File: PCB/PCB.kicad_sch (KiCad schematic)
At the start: 114 parts, among them J1 Termocouple_2, J10 2x5_2.54mm, J12 SSR2, J13 14x1-2.54mm, J14 USB_C_Receptacle_USB2.0, J2 PWR_IN, J3 Conn_01x02_Pin, J4 4x1-2.54mm, J5 Termocouple_1, J6 OUT2, J7 OUT1, J8 SSR1, Q1 BC817, Q2 BC817, Q3 BC817, Q4 BC817, Q5 AP30N03DF, SW1 SW_DPDT, SW2 SW_SPST, U1 MAX31855KASA, U2 MAX31855KASA, U4 MP2303ADN, U5 STM32F411CEUx, U6 CH340G, U7 W25Q16JVSNIQ, Y1 12MHz, Y3 12MHz

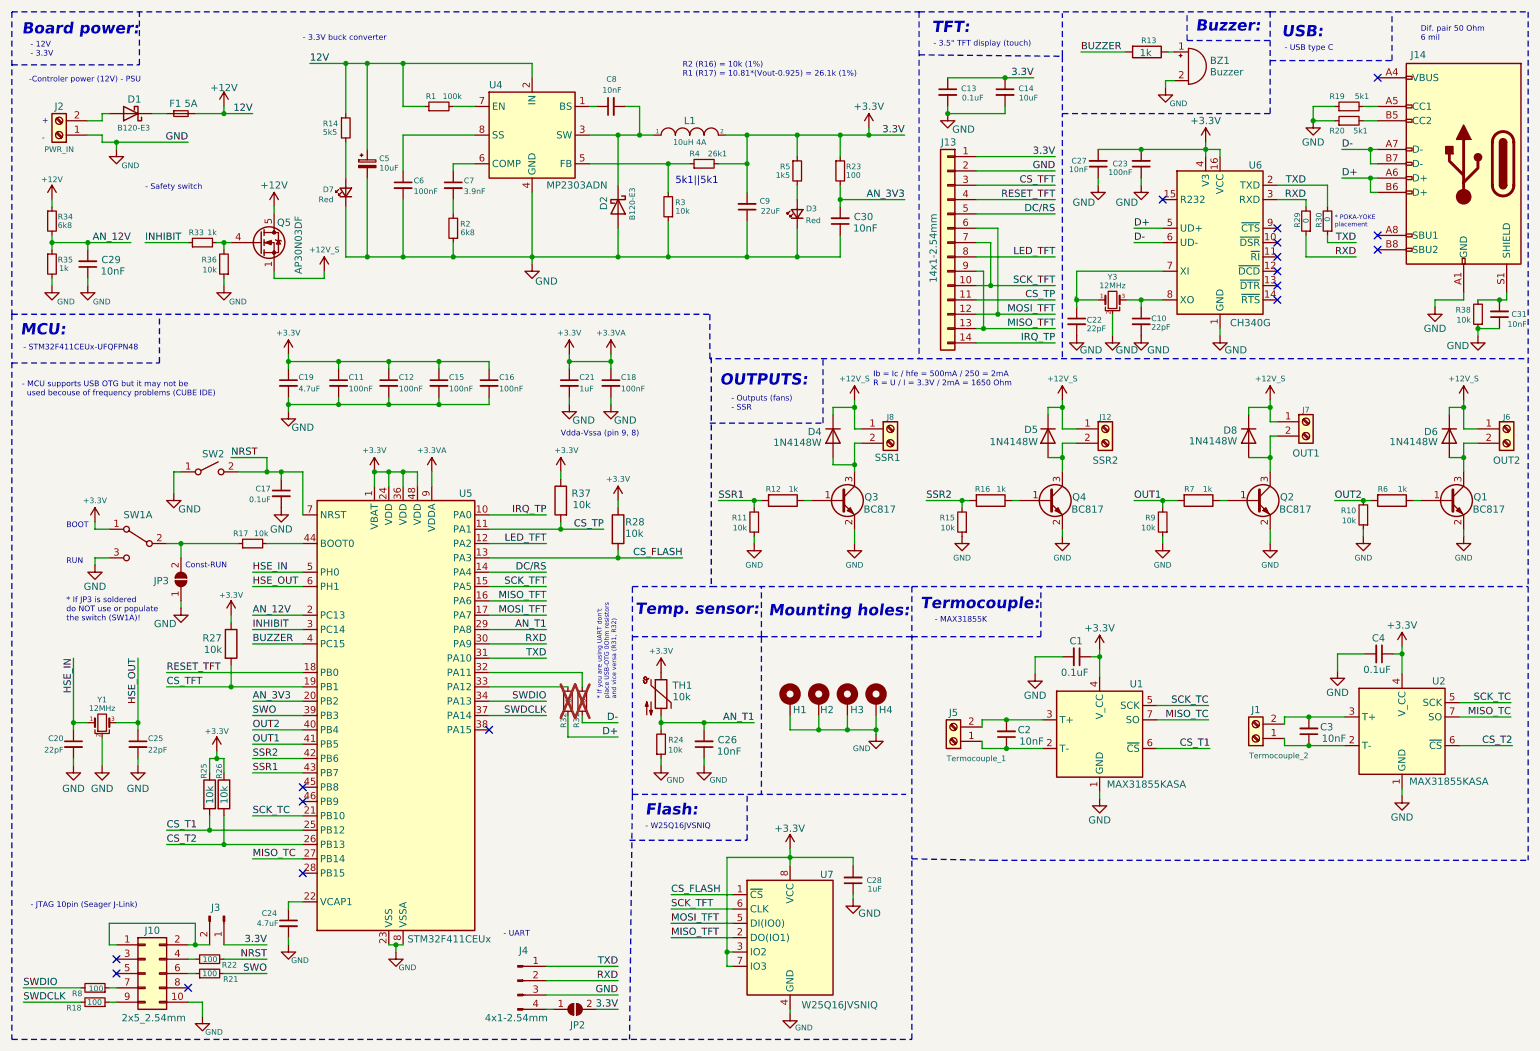
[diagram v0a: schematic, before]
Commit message: PCB done and ordered, touch screen and TFT works, flash works, EdternalLoader, GUI partialy done
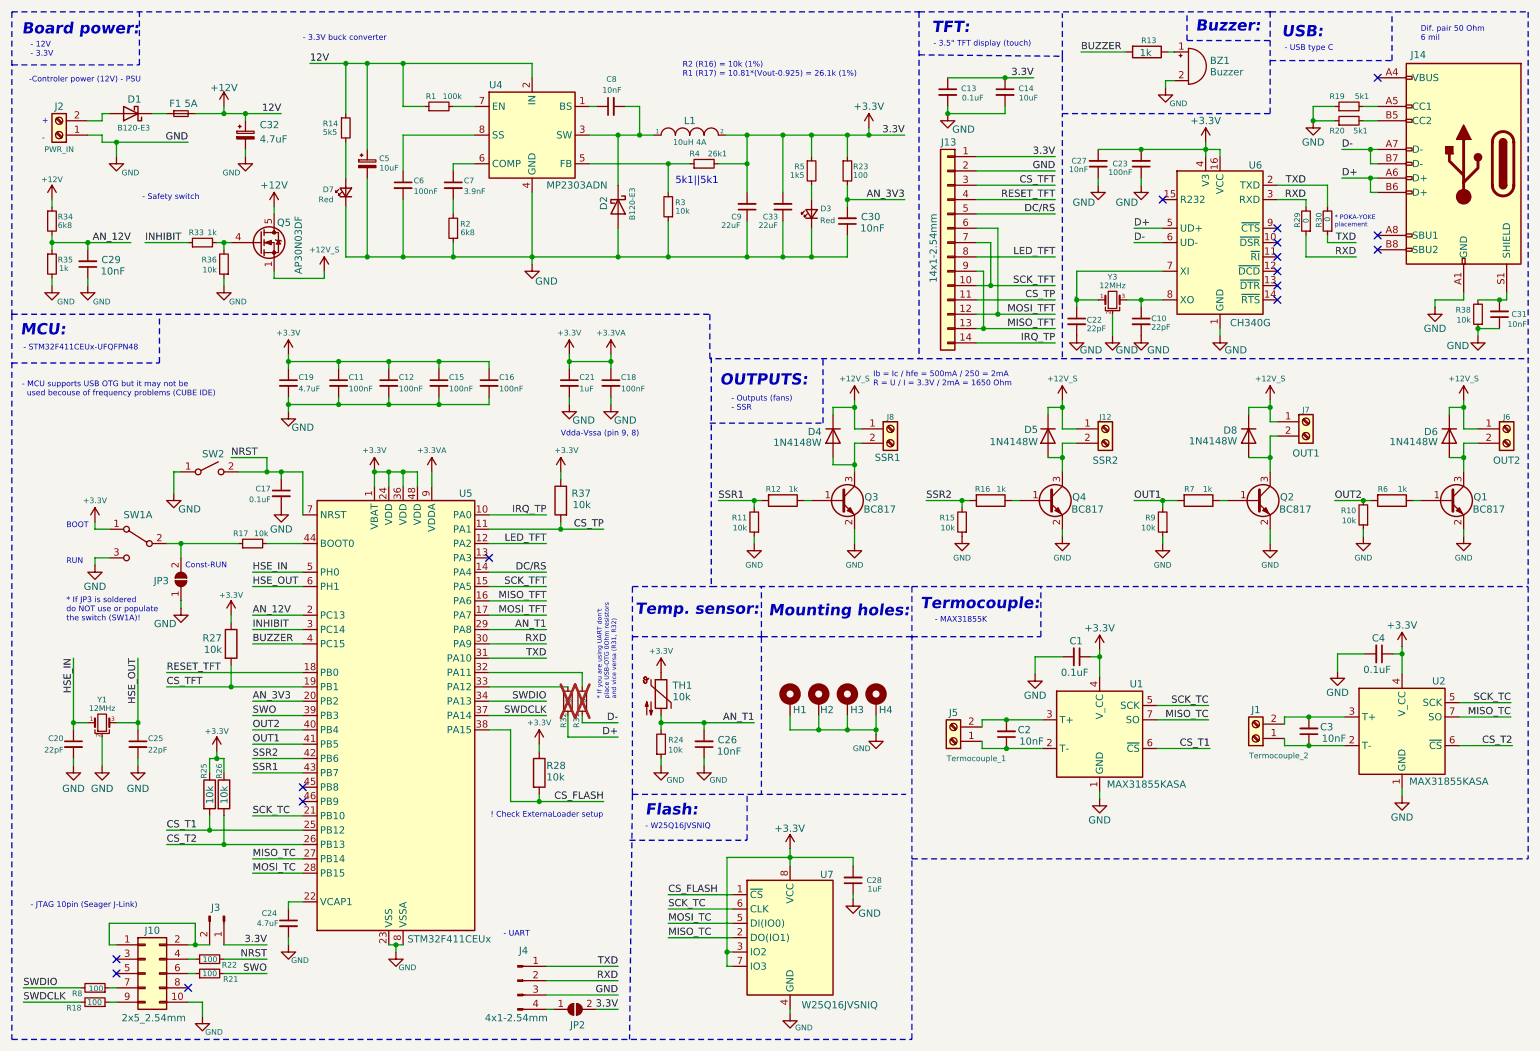
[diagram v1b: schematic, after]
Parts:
- added C32: 4.7uF, Capacitor_SMD:CP_Elec_4x5.4, symbol Device:C_Polarized_Small
- added C33: 22uF, Capacitor_SMD:C_1206_3216Metric, symbol Device:C_Small
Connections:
- net +12V: now also C32.1
- net +3.3V: now also C33.2
- net CS_FLASH: now also U5.38 (PA15); no longer U5.13 (PA3)
- net GND: now also C32.2, C33.1
- net MISO_TC: now also U7.2 (DO(IO1))
- net MISO_TFT: no longer U7.2 (DO(IO1))
- net MOSI_TFT: no longer U7.5 (DI(IO0))
- net SCK_TC: now also U7.6 (CLK)
- net SCK_TFT: no longer U7.6 (CLK)
- net MOSI_TC: now reaches U5.28 (PB15)
- net MOSI_TC: now also U7.5 (DI(IO0))
- no-connect marks 17 -> 16
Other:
- note added: "! Check ExternaLoader setup"
- moved on the sheet: C30, C9, D3, R23, R28, R5

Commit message: PCB works (Problems: safety switch, analog inputs mistake), ExternalLoader works, gui in progress
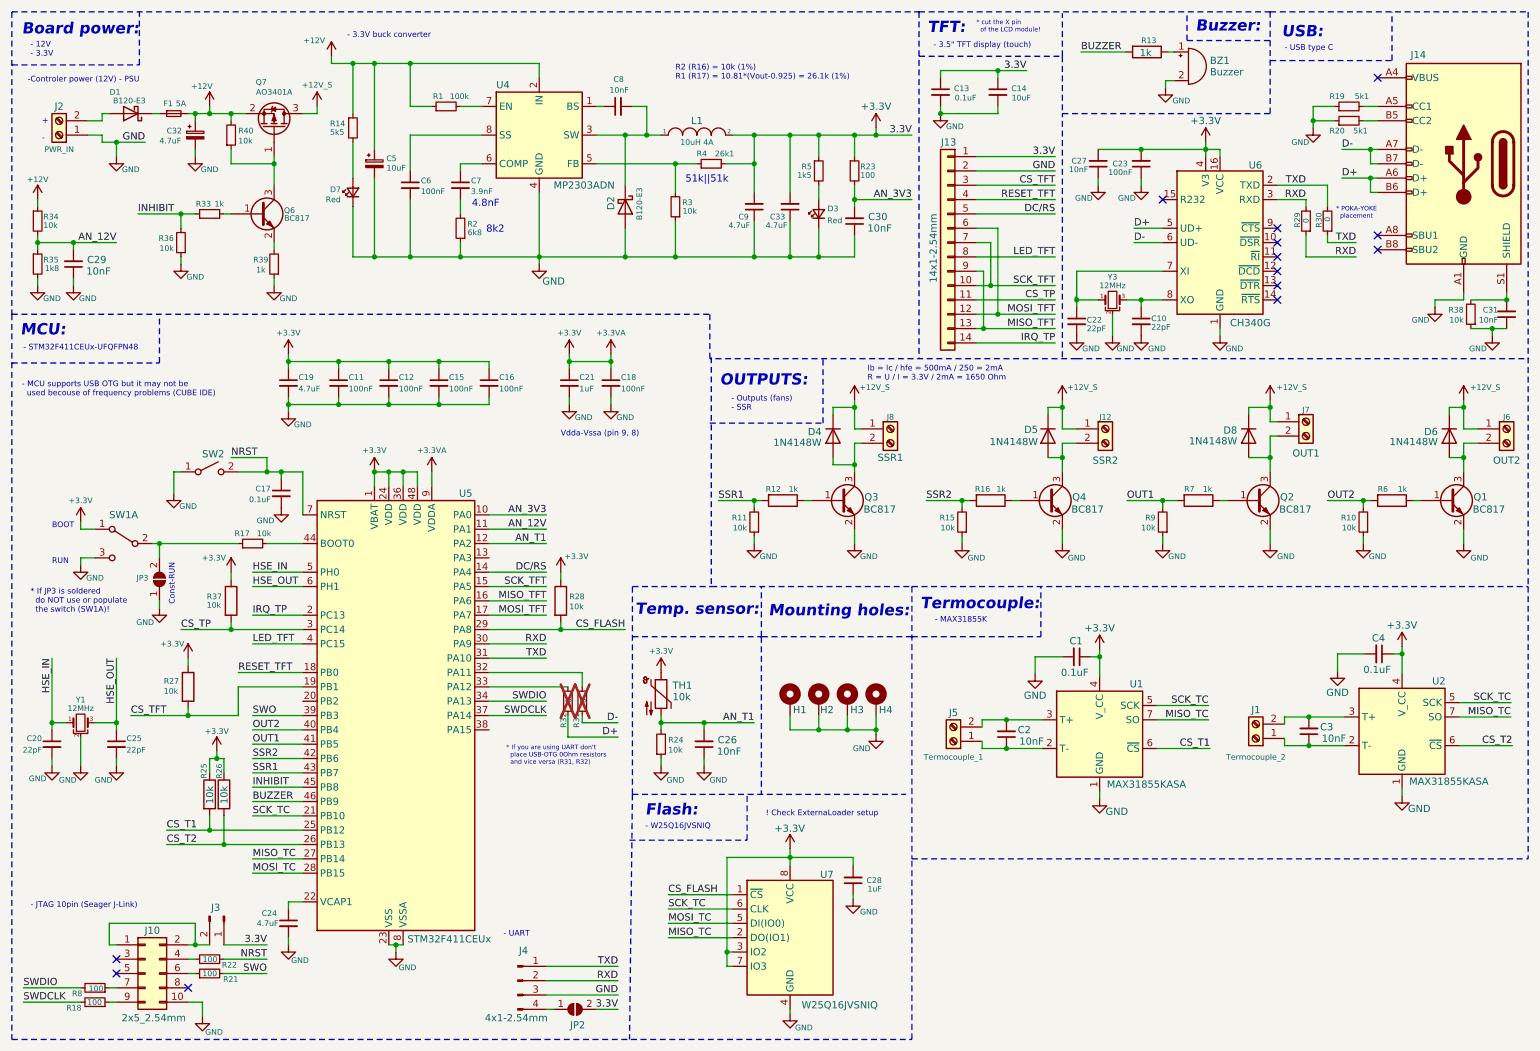
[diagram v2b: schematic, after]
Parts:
- removed Q5: AP30N03DF, Package_SON:Diodes_PowerDI3333-8, symbol Transistor_FET:DMN3008SFG
- added Q6: BC817, Package_TO_SOT_SMD:SOT-23, symbol Transistor_BJT:BC817
- added Q7: AO3401A, Package_TO_SOT_SMD:SOT-23, symbol Transistor_FET:AO3401A
- added R39: 1k, Resistor_SMD:R_0603_1608Metric, symbol Device:R_Small
- added R40: 10k, Resistor_SMD:R_0603_1608Metric, symbol Device:R_Small
- C26, C29, C30: footprint Capacitor_SMD:C_0603_1608Metric -> Capacitor_SMD:C_0402_1005Metric
- C33, C9: value 22uF -> 4.7uF
- R34: value 6k8 -> 10k
- R35: value 1k -> 1k8
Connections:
- net +12V: now also Q7.2 (S), R40.2
- net +12V_S: now also Q7.3 (D)
- net AN_12V: now also U5.11 (PA1); no longer U5.2 (PC13)
- net AN_3V3: now also U5.10 (PA0); no longer U5.20 (PB2)
- net AN_T1: now also U5.12 (PA2); no longer U5.29 (PA8)
- net BUZZER: now also U5.46 (PB9); no longer U5.4 (PC15)
- net CS_FLASH: now also U5.29 (PA8); no longer U5.38 (PA15)
- net CS_TP: now also U5.3 (PC14); no longer U5.11 (PA1)
- net GND: now also R39.1
- net INHIBIT: now also R36.2, U5.45 (PB8); no longer U5.3 (PC14)
- net IRQ_TP: now also U5.2 (PC13); no longer U5.10 (PA0)
- net LED_TFT: now also U5.4 (PC15); no longer U5.12 (PA2)
- net at R33.2: now also Q6.1 (B); no longer R36.2
- new net: Q6.2 (E), R39.2
- new net: Q6.3 (C), Q7.1 (G), R40.1
- no-connect marks 16 -> 13
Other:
- note added: "* cut the X pin of the LCD module!"
- note added: "4.8nF"
- note added: "51k||51k"
- note added: "8k2"
- note removed: "- Safety switch"
- note removed: "5k1||5k1"
- note removed: "Dif. pair 50 Ohm 6 mil"
- moved on the sheet: C13, C14, C20, C25, C29, C30, C31, C32, C33, C5, C6, C7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

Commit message: PCB update, firmaware
usb problem -> repaired

firmware update: pid, PWM, gui
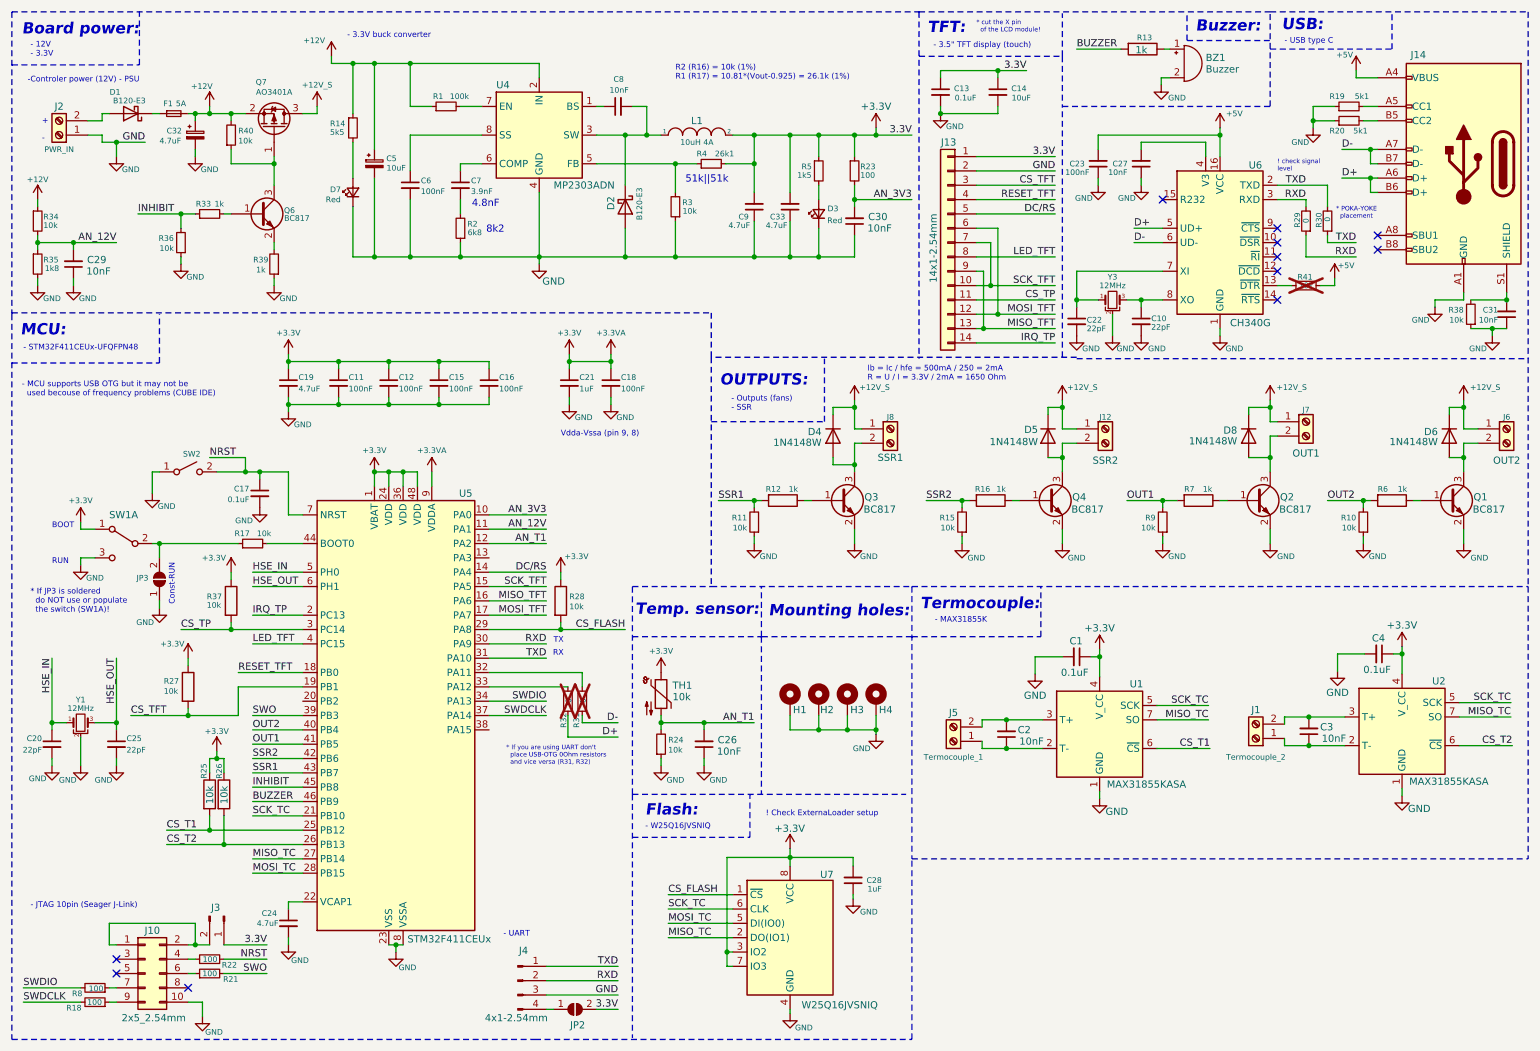
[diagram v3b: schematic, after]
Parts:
- added R41: 10k, Resistor_SMD:R_0603_1608Metric, symbol Device:R_Small
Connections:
- net +3.3V: no longer C23.2, C27.2, U6.16 (VCC), U6.4 (V3)
- net +5V: now reaches J14.A4 (VBUS), J14.A9 (VBUS), J14.B4 (VBUS), J14.B9 (VBUS)
- net +5V: now also C23.2, U6.16 (VCC), R41.1
- net at U6.13 (~{DTR}): now also R41.2
- new net: C27.2, U6.4 (V3)
- no-connect marks 13 -> 11
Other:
- note added: "! check signal level"
- note added: "RX"
- note added: "TX"
- moved on the sheet: BZ1, C17, C23, R13, SW2
